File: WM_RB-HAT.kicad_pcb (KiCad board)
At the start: 2 copper layers, 65 x 40.5 mm, 80 parts, among them J1 Line R, J2 Output Stereo, J3 2x20 Pins, J5 Output Mono, J7 Line L, Q1 BC817, U1 WM8960, U4 MCP1711T-33 /OT

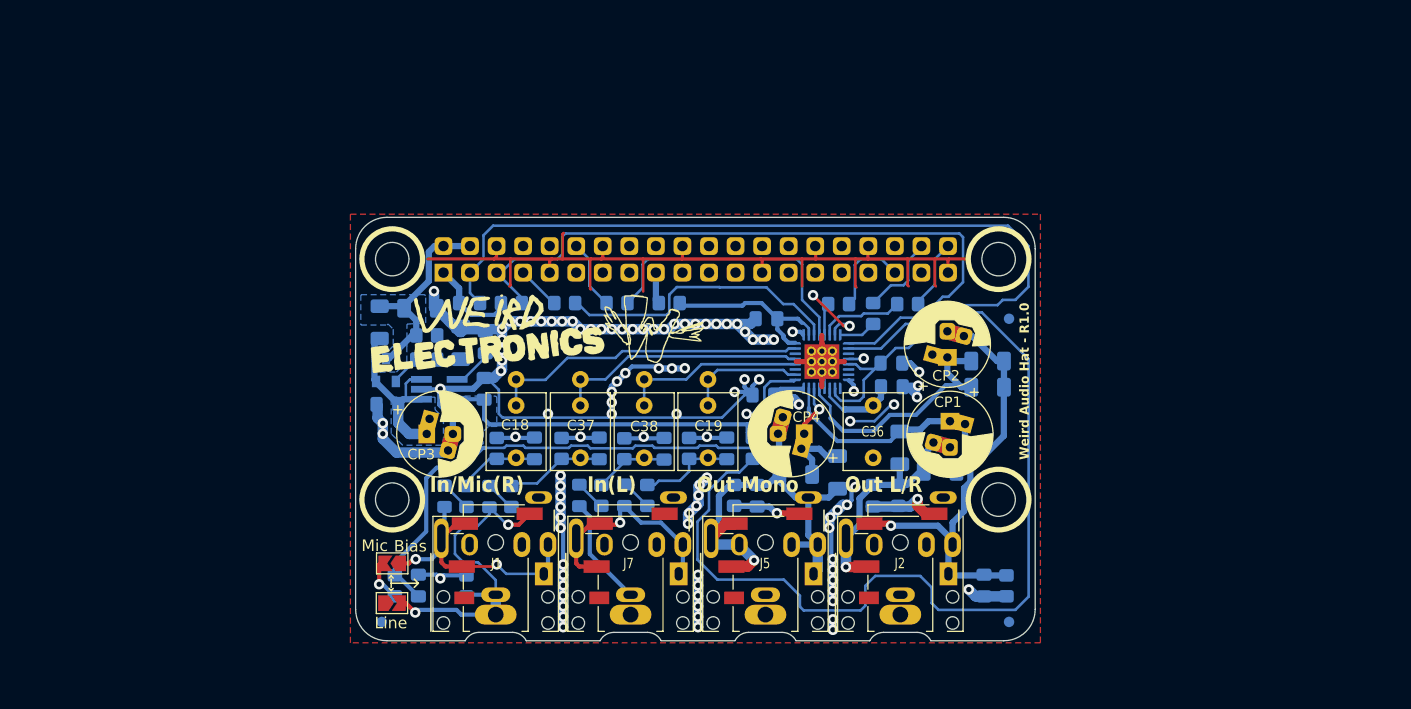
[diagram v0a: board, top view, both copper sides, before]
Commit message: WIP v1.1: SMD migration + input simplification
- Remove differential input stage, simplify jacks
- Migrate to 0603, remove HandSolder footprints
- Add LCSC codes, 4-layer stackup config
- Add SMD libs and design docs
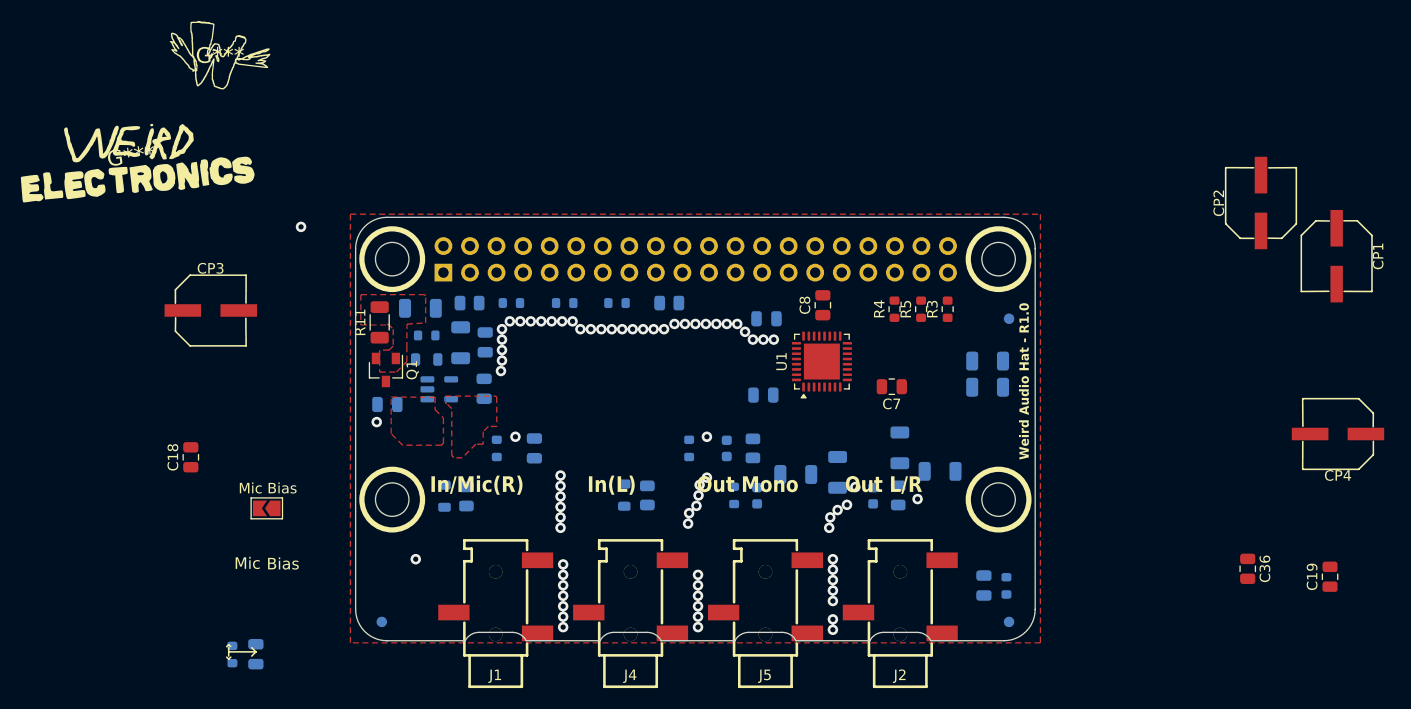
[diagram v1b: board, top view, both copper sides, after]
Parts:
- removed C33, C34: pf, Capacitor_SMD:C_0805_2012Metric_Pad1.18x1.45mm_HandSolder
- removed C37, C38: 1u Film P5-7.5mm W<6mm, ArduinoModules:C_Rect_Film_L7.2mm_W5.5mm_P5.00mm_7.5mm_Combo_FKS2_FKP2_MKS2_MKP2
- removed FB6, FB7: 220-1k, Inductor_SMD:L_0805_2012Metric_Pad1.15x1.40mm_HandSolder
- removed J7: Line L, ArduinoModules:Jack_3.5mm_Combo_CUI_SJ1-3525N_Horizontal
- removed JP3: Line, ArduinoModules:SolderJumper-2_P1.3mm_Open_TrianglePad1.0x1.5mm
- removed R25: 1k, Resistor_SMD:R_0805_2012Metric_Pad1.20x1.40mm_HandSolder
- removed R28, R29: 100R, Resistor_SMD:R_0805_2012Metric_Pad1.20x1.40mm_HandSolder
- removed R30, R31: 100K, Resistor_SMD:R_0805_2012Metric_Pad1.20x1.40mm_HandSolder
- added J4: AudioJack3, libs:AUDIO-SMD_PJ-320B, F.Cu at (104.8, 96.6)
- C11, C13, C14, C15, C16, C17, C22, C35: footprint ArduinoModules:C_1206_3216Metric_Pad1.33x1.80mm_HandSolder -> Capacitor_SMD:C_1206_3216Metric
- C12, C2, C3, C31, C32, C5: footprint Capacitor_SMD:C_0805_2012Metric_Pad1.18x1.45mm_HandSolder -> Capacitor_SMD:C_0805_2012Metric
- C18, C19: value 1u Film P5-7.5mm W<6mm -> 1uF X7R; footprint ArduinoModules:C_Rect_Film_L7.2mm_W5.5mm_P5.00mm_7.5mm_Combo_FKS2_FKP2_MKS2_MKP2 -> Capacitor_SMD:C_0805_2012Metric
- C20, C30, C9: value pf -> 390p; footprint Capacitor_SMD:C_0805_2012Metric_Pad1.18x1.45mm_HandSolder -> Capacitor_SMD:C_0603_1608Metric
- C21, C29: value pf -> 390p; footprint Capacitor_SMD:C_0805_2012Metric_Pad1.18x1.45mm_HandSolder -> Capacitor_SMD:C_0805_2012Metric
- C36: value 1u Film P5mm W<6mm -> 1uF X7R; footprint Capacitor_THT:C_Rect_L7.2mm_W5.5mm_P5.00mm_FKS2_FKP2_MKS2_MKP2 -> Capacitor_SMD:C_0805_2012Metric
- C7: value 4.7u -> 390p; footprint Capacitor_SMD:C_0805_2012Metric_Pad1.18x1.45mm_HandSolder -> Capacitor_SMD:C_0805_2012Metric; moved to F.Cu
- C8: footprint Capacitor_SMD:C_0805_2012Metric_Pad1.18x1.45mm_HandSolder -> Capacitor_SMD:C_0805_2012Metric; moved to F.Cu
- CP1, CP2, CP4: value 22-68uF Bipolar 25-35V -> 220uF 16V; footprint ArduinoModules:CP_Radial_D8.0mm_P2.50-3.5mm_100uF_Mejores_Pads -> libs:CAP-SMD_BD6.3-L6.6-W6.6-FD
- CP3: value 100-470uF 6.3V -> 220uF 16V; footprint ArduinoModules:CP_Radial_D8.0mm_P2.50-3.5mm_100uF_Mejores_Pads -> libs:CAP-SMD_BD6.3-L6.6-W6.6-FD
- FB1, FB2, FB3: footprint Inductor_SMD:L_0805_2012Metric_Pad1.15x1.40mm_HandSolder -> Inductor_SMD:L_0805_2012Metric
- J1: value Line R -> AudioJack3; footprint ArduinoModules:Jack_3.5mm_Combo_CUI_SJ1-3525N_Horizontal -> libs:AUDIO-SMD_PJ-320B
- J2: value Output Stereo -> AudioJack3; footprint ArduinoModules:Jack_3.5mm_Combo_CUI_SJ1-3525N_Horizontal -> libs:AUDIO-SMD_PJ-320B
- J5: value Output Mono -> AudioJack3; footprint ArduinoModules:Jack_3.5mm_Combo_CUI_SJ1-3525N_Horizontal -> libs:AUDIO-SMD_PJ-320B
- Q1: moved to F.Cu
- R10, R14, R27, R9: footprint Resistor_SMD:R_0805_2012Metric_Pad1.20x1.40mm_HandSolder -> Resistor_SMD:R_0805_2012Metric
- R11: footprint ArduinoModules:R_1206_3216Metric_Pad1.30x1.75mm_HandSolder -> Resistor_SMD:R_1206_3216Metric; moved to F.Cu
- R12, R13, R15, R7, R8: footprint Resistor_SMD:R_0805_2012Metric_Pad1.20x1.40mm_HandSolder -> Resistor_SMD:R_0603_1608Metric
- R2, R26: value 10R -> 270; footprint Resistor_SMD:R_0805_2012Metric_Pad1.20x1.40mm_HandSolder -> Resistor_SMD:R_0603_1608Metric
- R22, R6: value 10K -> 100K; footprint Resistor_SMD:R_0805_2012Metric_Pad1.20x1.40mm_HandSolder -> Resistor_SMD:R_0603_1608Metric
- R23: value 10K -> 100K; footprint Resistor_SMD:R_0805_2012Metric_Pad1.20x1.40mm_HandSolder -> Resistor_SMD:R_0805_2012Metric
- R24: value 1K -> 100R; footprint Resistor_SMD:R_0805_2012Metric_Pad1.20x1.40mm_HandSolder -> Resistor_SMD:R_0805_2012Metric
- R3, R4, R5: value 10R -> 270; footprint Resistor_SMD:R_0805_2012Metric_Pad1.20x1.40mm_HandSolder -> Resistor_SMD:R_0603_1608Metric; moved to F.Cu
- U1: footprint ArduinoModules:QFN-32-1EP_5x5mm_P0.5mm_EP3.3x3.3mm_Handsolder -> Package_DFN_QFN:QFN-32-1EP_5x5mm_P0.5mm_EP3.45x3.45mm; moved to F.Cu
- U4: footprint Package_TO_SOT_SMD:TSOT-23-5_HandSoldering -> Package_TO_SOT_SMD:TSOT-23-5
- moved C19 60.6 mm to (171.7, 94.7)
- moved CP4 51.1 mm to (172.5, 81.0)
- moved G*** 49.0 mm to (65.5, 44.8)
- moved CP1 40.2 mm to (172.3, 64.0)
- moved C36 39.1 mm to (163.8, 93.9)
- moved G*** 37.2 mm to (57.0, 54.4)
- moved CP2 33.4 mm to (165.1, 58.9)
- moved C18 31.1 mm to (62.7, 83.3)
- moved CP3 23.8 mm to (64.6, 69.2)
- moved C2 16.9 mm to (69.0, 102.1)
- moved R15 16.9 mm to (66.7, 102.1)
- moved JP1 13.1 mm to (70.1, 88.1)
- moved C8 8.59 mm to (123.2, 68.7), turned to 90 degrees
- moved R4 5.37 mm to (130.0, 69.1), turned to 90 degrees
- moved R5 4.61 mm to (132.6, 69.1)
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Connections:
- J1 pad S: Net-(JP3-B) -> GND
- J2 pad R: /HP_R_AC -> /OUT_MONO_AC
- J2 pad T: /HP_L_AC -> /OUT_MONO_AC
- J5 pad R: /OUT_MONO_AC -> Net-(FB2-Pad1)
- J5 pad T: /OUT_MONO_AC -> Net-(FB2-Pad1)
- U1 pad 4: /GND_INPUT_L -> unconnected-(U1-LINPUT1-Pad4)
- U1 pad 5: /GND_INPUT_R -> unconnected-(U1-RINPUT1-Pad5)
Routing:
- net GND: track 303.5 -> 0.00 mm, vias 104 -> 74
- net Net-(U1-SPKVDD1): track 103.9 -> 0.00 mm
- net /I2C_SDA: track 84.3 -> 0.00 mm
- net /I2C_SCL: track 70.1 -> 0.00 mm
- net /MICBIAS: track 58.8 -> 0.00 mm, vias 2 -> 0
- net /OUT_MONO_AC: track 44.7 -> 0.00 mm, vias 1 -> 0
- net /HP_L_AC: track 42.8 -> 0.00 mm, vias 1 -> 0
- net +3.3VA: track 37.8 -> 0.00 mm
- net Net-(JP3-B): track 32.1 -> 0.00 mm, vias 2 -> 0
- net /LINE_INPUT_R: track 30.5 -> 0.00 mm
- net /CLK: track 27.9 -> 0.00 mm
- net Net-(U1-BCLK): track 27.4 -> 0.00 mm
- net Net-(JP1-A): track 26.8 -> 0.00 mm, vias 2 -> 1
- net /HP_L: track 25.0 -> 0.00 mm
- net /GND_INPUT_R: track 24.1 -> 0.00 mm
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- added copper zone on F.Cu, net +3.3VA
- added copper zone on F.Cu, net +5V
- added copper zone on F.Cu, net +VREGIN
- added copper zone on In1.Cu, net GND
- removed copper zone on B.Cu, net +3.3VA
- removed copper zone on B.Cu, net +5V
- removed copper zone on B.Cu, net +VREGIN
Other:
- copper layers 2 -> 4
- rule pad_to_mask_clearance: 0.1 -> 0.05
- board text added: "${REFERENCE}"
- board text removed: "Crosstalk @-60dB alejar o meter componente como shield."
- board text removed: "Mas profunco"

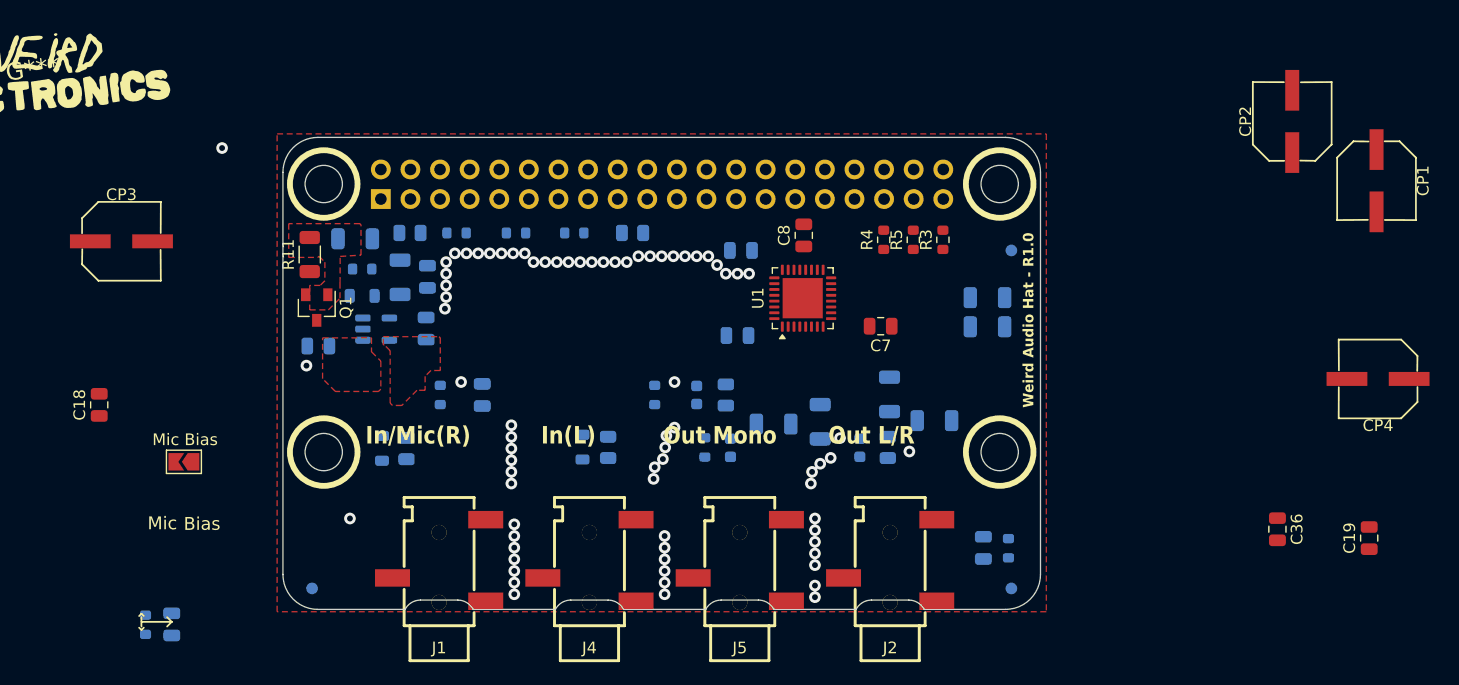
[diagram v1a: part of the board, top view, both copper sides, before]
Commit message: Update PCB from schematic
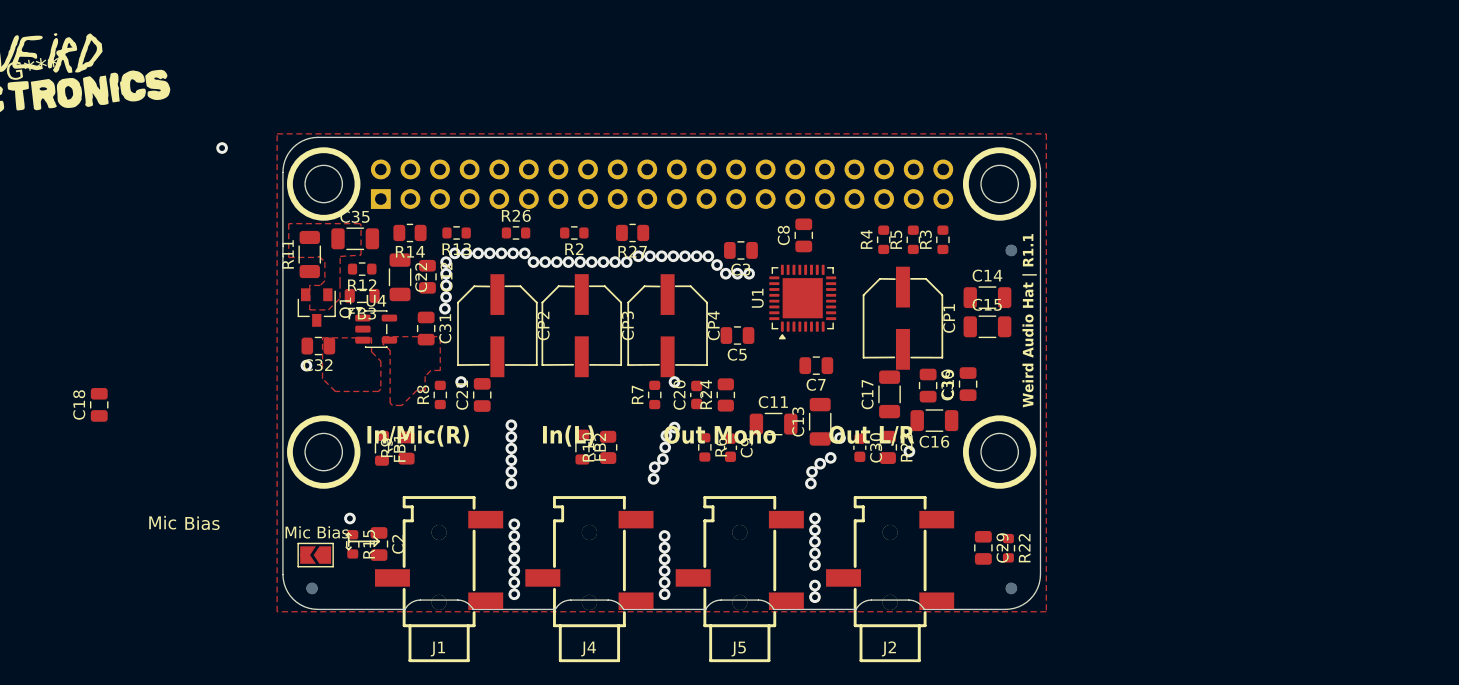
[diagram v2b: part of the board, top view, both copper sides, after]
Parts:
- C11, C12, C13, C14, C15, C16, C17, C2, C20, C21, C22, C29, C3, C30, C31, C32, C35, C5, C9, FB1, FB2, FB3, R10, R12, R13, R14, R15, R2, R22, R23, R24, R26, R27, R6, R7, R8, R9, U4: moved to F.Cu
- moved CP2 70.4 mm to (96.9, 76.5), turned to -90 degrees
- moved CP4 61.1 mm to (111.5, 76.5), turned to -90 degrees
- moved CP1 42.3 mm to (131.7, 75.8)
- moved CP3 40.2 mm to (104.1, 76.5), turned to -90 degrees
- moved C19 36.9 mm to (137.3, 81.5)
- moved C36 32.4 mm to (133.9, 81.6)
- moved C2 19.1 mm to (86.7, 95.2), turned to -90 degrees
- moved R15 19.1 mm to (84.5, 95.2), turned to -90 degrees
- moved JP1 13.8 mm to (81.4, 96.1)
- moved C7 6.47 mm to (124.3, 79.9)
- turned R9 to 90 degrees
- turned C12 to -90 degrees
- turned C13 to 90 degrees
- turned C17 to 90 degrees
- turned C20 to 90 degrees
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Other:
- board text added: "Weird Audio Hat | R1.1"
- board text removed: "Weird Audio Hat - R1.0"

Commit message: WIP: PCB and schematic progress
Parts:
- removed C11, C13, C14, C15, C16, C17: 47uF 35V 1206, Capacitor_SMD:C_1206_3216Metric
- moved CP2 60.3 mm to (138.4, 120.2)
- moved C18 56.4 mm to (111.5, 111.7)
- moved C19 55.8 mm to (93.5, 116.0)
- moved CP1 47.2 mm to (147.2, 120.4)
- moved C20 42.4 mm to (88.5, 116.2)
- moved R7 42.4 mm to (84.9, 116.2)
- moved R23 41.6 mm to (139.4, 127.5)
- moved C30 41.1 mm to (135.1, 127.4)
- moved FB2 37.3 mm to (89.6, 121.2)
- moved R10 37.3 mm to (91.8, 121.2)
- moved CP4 37.2 mm to (122.8, 111.9)
- moved C2 36.3 mm to (109.2, 123.7)
- moved JP1 35.7 mm to (108.8, 118.9)
- moved R15 35.7 mm to (111.9, 118.0)
- moved C29 33.5 mm to (144.7, 128.5)
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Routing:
- net GND: vias 74 -> 70
- added copper zone on In2.Cu, net +5V
- added copper zone on In2.Cu, net +VREGIN
- removed copper zone on F.Cu, net +3.3VA
- removed copper zone on F.Cu, net +5V
- removed copper zone on F.Cu, net +VREGIN

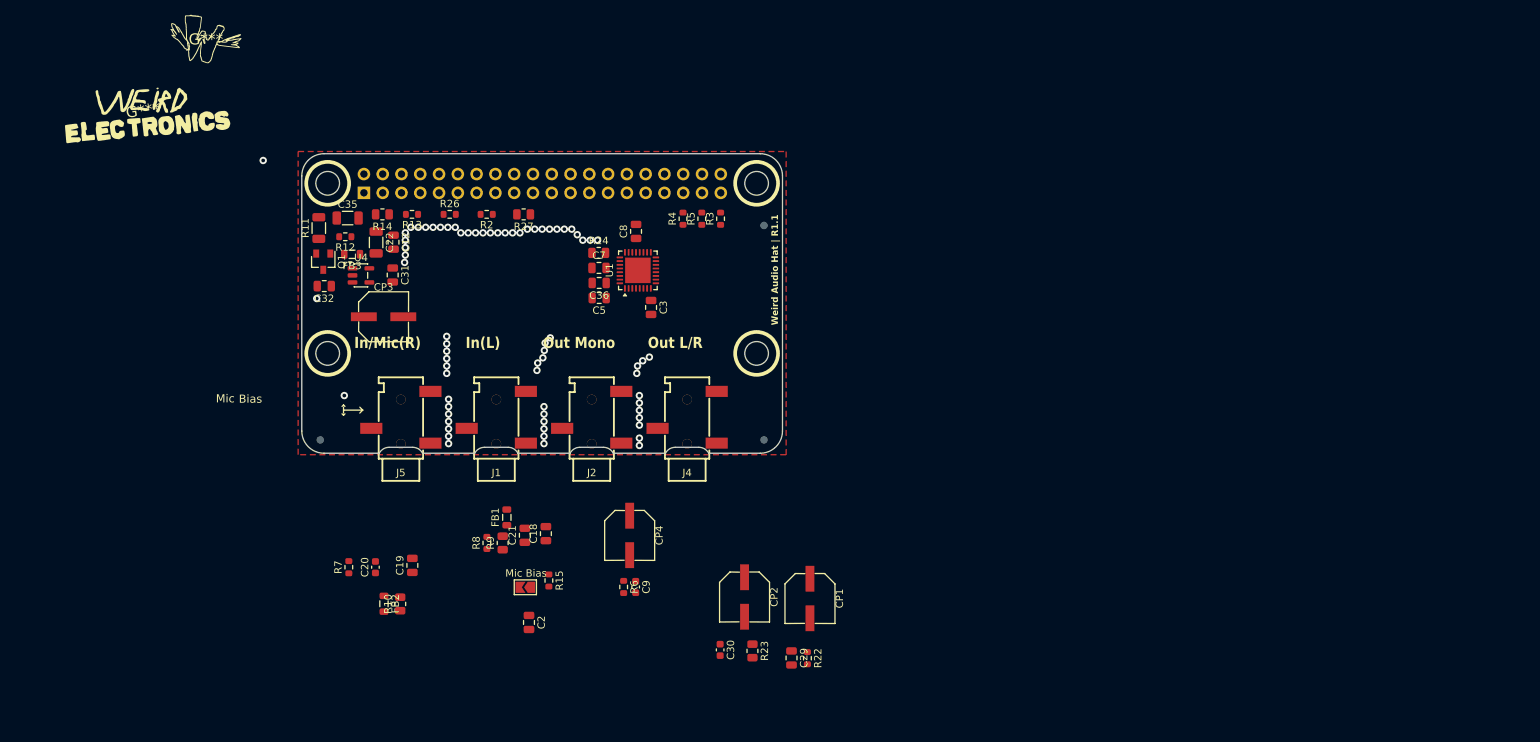
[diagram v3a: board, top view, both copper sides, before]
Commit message: WIP: 4-layer SIG/GND/GND/SIG stackup + SMD migration progress
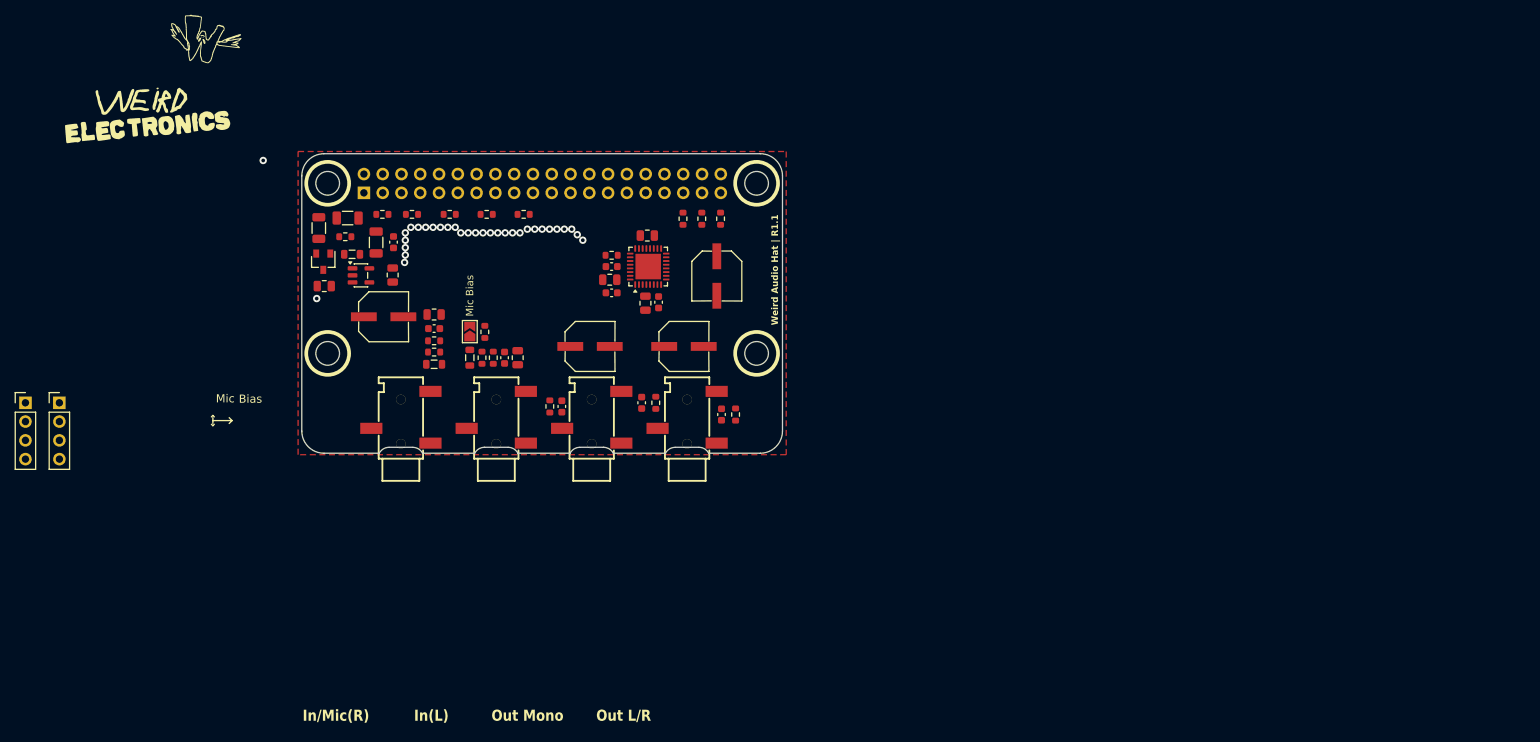
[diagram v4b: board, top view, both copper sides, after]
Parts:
- removed FM1, FM2, FM3: Fiducial, ArduinoModules:Fiducial_1mm_Mask2mm
- added J6: Audio In, Connector_PinHeader_2.54mm:PinHeader_1x04_P2.54mm_Vertical, F.Cu at (41.1, 94.0)
- added J7: Audio Out, Connector_PinHeader_2.54mm:PinHeader_1x04_P2.54mm_Vertical, F.Cu at (45.7, 94.0)
- C12, C21, C29, C3, C5, C7: footprint Capacitor_SMD:C_0805_2012Metric -> Capacitor_SMD:C_0603_1608Metric
- R10, R14, R23, R24, R27, R9: footprint Resistor_SMD:R_0805_2012Metric -> Resistor_SMD:R_0603_1608Metric
- moved C2 46.0 mm to (125.0, 80.5)
- moved CP1 45.4 mm to (134.6, 76.8)
- moved R23 36.0 mm to (126.4, 94.0)
- moved JP1 35.3 mm to (101.2, 84.5), turned to 90 degrees
- moved C30 35.1 mm to (124.5, 94.0)
- moved CP2 34.9 mm to (130.2, 86.4), turned to 0 degrees
- moved R15 34.7 mm to (103.3, 84.4)
- moved R10 34.4 mm to (96.4, 87.1), turned to 180 degrees
- moved R22 34.4 mm to (137.2, 95.6), turned to 90 degrees
- moved C29 34.3 mm to (135.3, 95.6), turned to 90 degrees
- moved C19 34.1 mm to (96.4, 82.0), turned to 180 degrees
- moved C20 33.2 mm to (96.4, 83.9), turned to 0 degrees
- moved FB2 33.1 mm to (96.4, 88.8), turned to 180 degrees
- moved R7 32.7 mm to (96.4, 85.6), turned to 0 degrees
- moved R6 26.4 mm to (112.0, 94.5)
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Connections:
- net Net-(FB2-Pad1) renamed /INPUT_L
- net Net-(JP1-A) renamed /INPUT_R
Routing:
- net GND: vias 70 -> 32
- net /INPUT_R: vias 1 -> 0
